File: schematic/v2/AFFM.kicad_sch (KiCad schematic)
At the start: 19 parts, among them J13 STEREO_OUT, J14 STEREO_IN, K1 DIPxx-1Axx-11x, K2 DIPxx-1Axx-11x, K3 DIPxx-1Axx-11x, K4 DIPxx-1Axx-11x

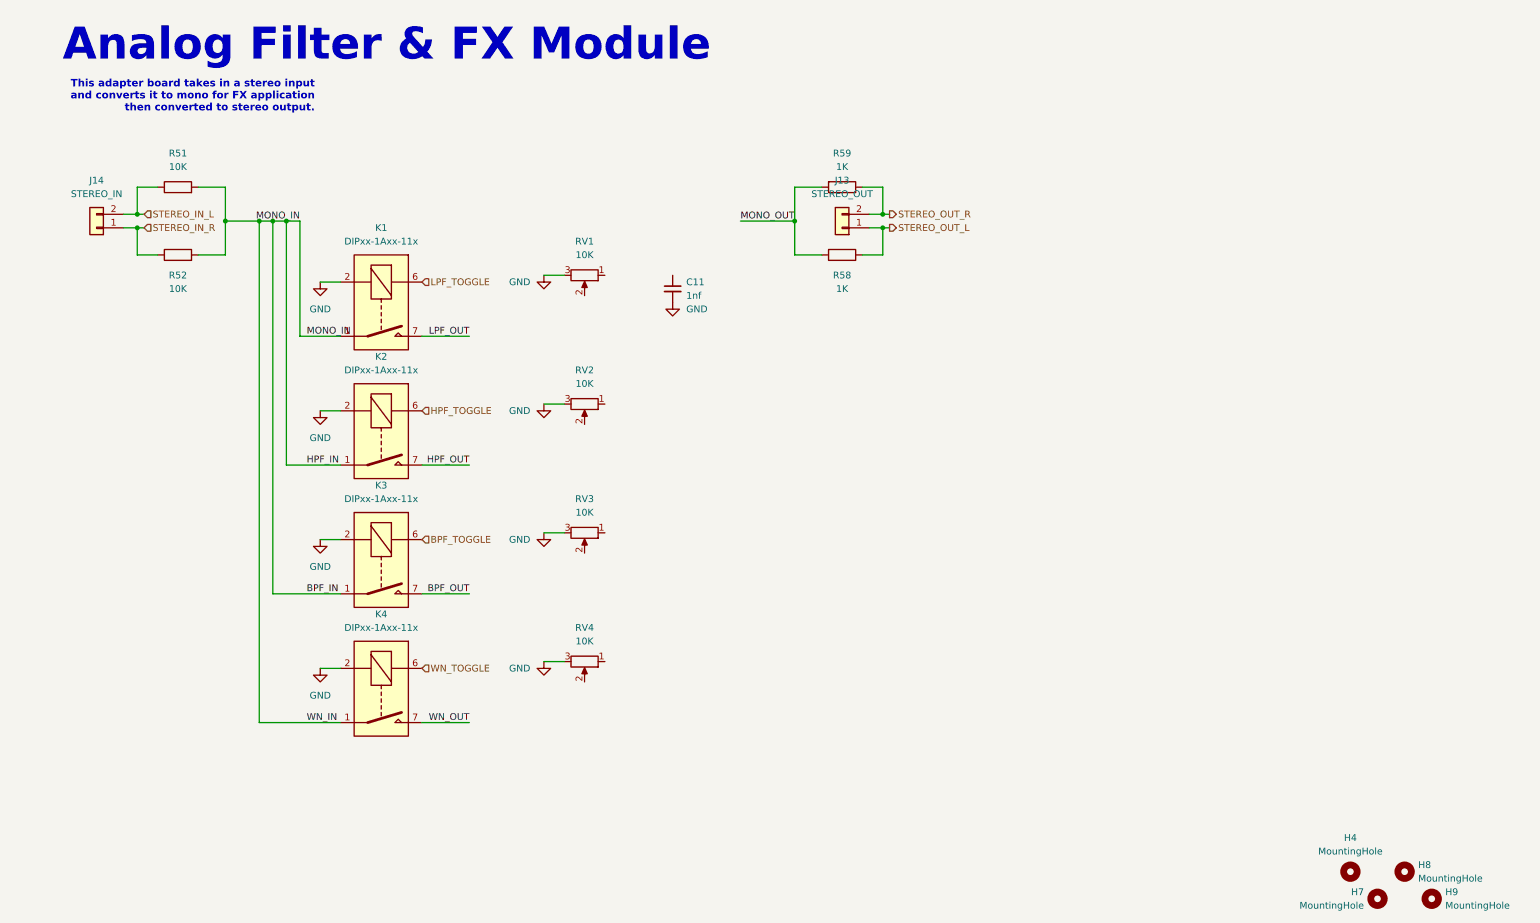
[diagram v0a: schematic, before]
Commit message: need to learn more about variable lpf, wiring, minimal capacitor for the circuit and cutoff with series resistor
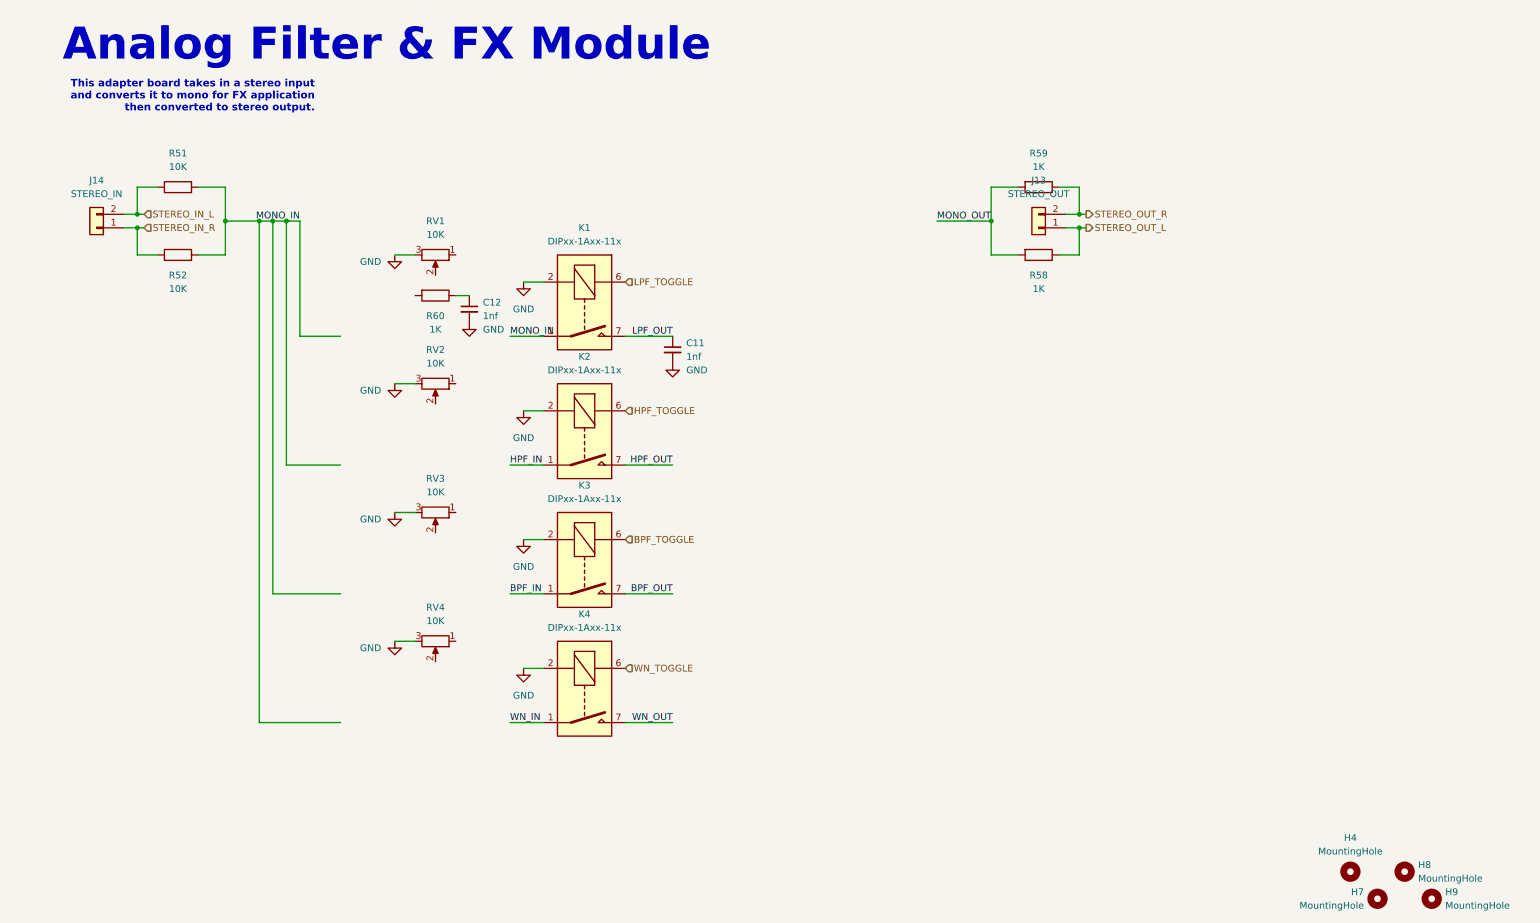
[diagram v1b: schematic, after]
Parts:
- added C12: 1nf, Capacitor_SMD:C_0805_2012Metric, symbol Device:C_Small
- added R60: 1K, Resistor_SMD:R_0805_2012Metric_Pad1.20x1.40mm_HandSolder, symbol Device:R
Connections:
- net BPF_IN: no longer K1.1, K1.14, K2.1, K2.14, K4.1, K4.14, R51.2, R52.2
- net GND: now also C12.2
- net LPF_OUT: now also C11.1
- new net: C12.1, R60.1
- new net HPF_IN: K2.1, K2.14
- new net MONO_IN: K1.1, K1.14, R51.2, R52.2
- new net WN_IN: K4.1, K4.14
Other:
- moved on the sheet: C11, J13, K1, K2, K3, K4, R58, R59, RV1, RV2, RV3, RV4

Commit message: schematic updates for affm
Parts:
- removed R60: 1K, Resistor_SMD:R_0805_2012Metric_Pad1.20x1.40mm_HandSolder, symbol Device:R
- C12: value 1nf -> 680pf
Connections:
- net GND: no longer RV1.3
- net MONO_IN: now also C12.1, RV1.1
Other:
- moved on the sheet: C12, RV1, RV2
